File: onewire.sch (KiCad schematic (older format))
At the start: 8 parts, among them J801 Conn_01x03, U801 RCLAMP0524P-N

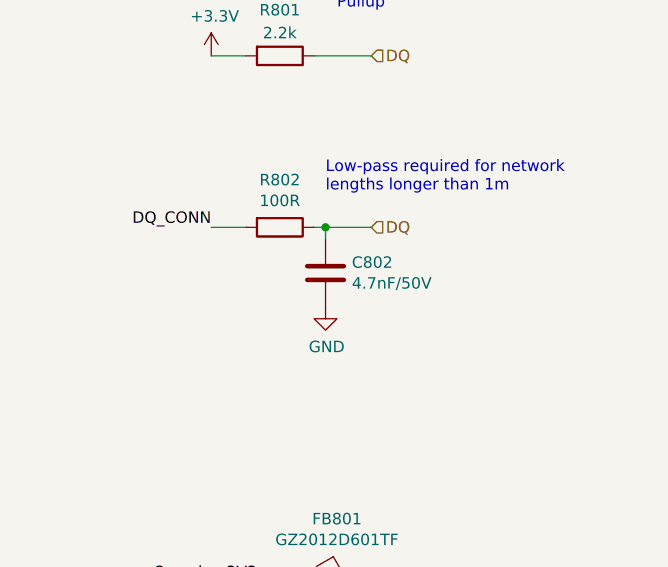
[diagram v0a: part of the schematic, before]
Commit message: Reduce 1-wire RC filter capacitor value
RC filter design guidelines were from a 5V system and from a driver
that could probably drive the line harder than the ESP32. Reduce
the filter cap to 1uF for a better performance.
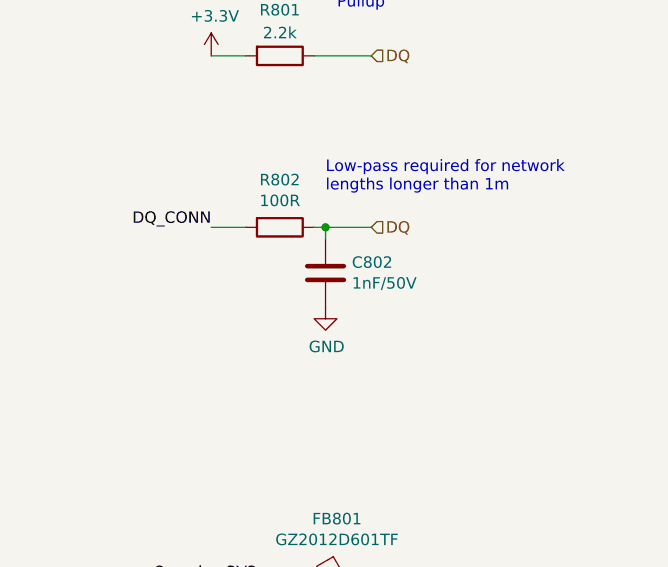
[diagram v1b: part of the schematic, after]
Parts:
- C802: value 4.7nF/50V -> 1nF/50V; LCSC C53987 -> C1588
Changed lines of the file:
@@
 P 4600 2550
 F 0 "C802" H 4715 2596 50  0000 L CNN
-F 1 "4.7nF/50V" H 4715 2505 50  0000 L CNN
+F 1 "1nF/50V" H 4715 2505 50  0000 L CNN
 F 2 "Capacitor_SMD:C_0603_1608Metric" H 4638 2400 50  0001 C CNN
 F 3 "~" H 4600 2550 50  0001 C CNN
-F 4 "C53987" H 4600 2550 50  0001 C CNN "LCSC"
+F 4 "C1588" H 4600 2550 50  0001 C CNN "LCSC"
 	1    4600 2550
 	1    0    0    -1
